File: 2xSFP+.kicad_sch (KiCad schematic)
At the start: 55 parts, among them J2 Bel-Fuse_SFP+_2x20_SS-79100-0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, U5 PCA9539AHF

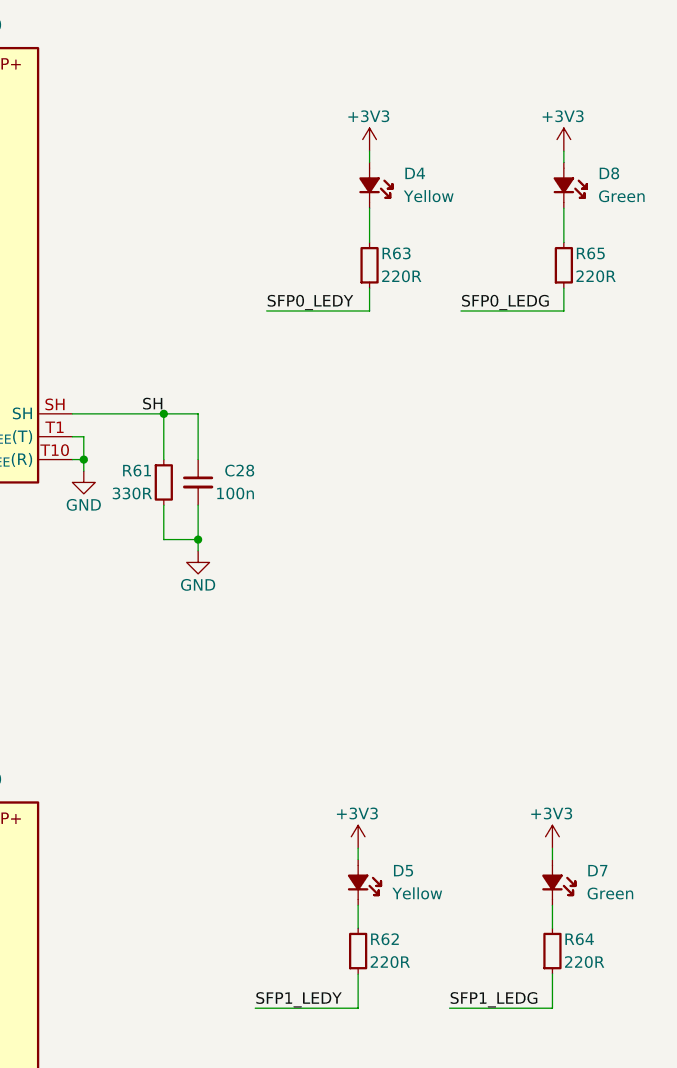
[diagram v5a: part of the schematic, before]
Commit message: [#66613] Change yellow LEDs from 0402 to 0603 package
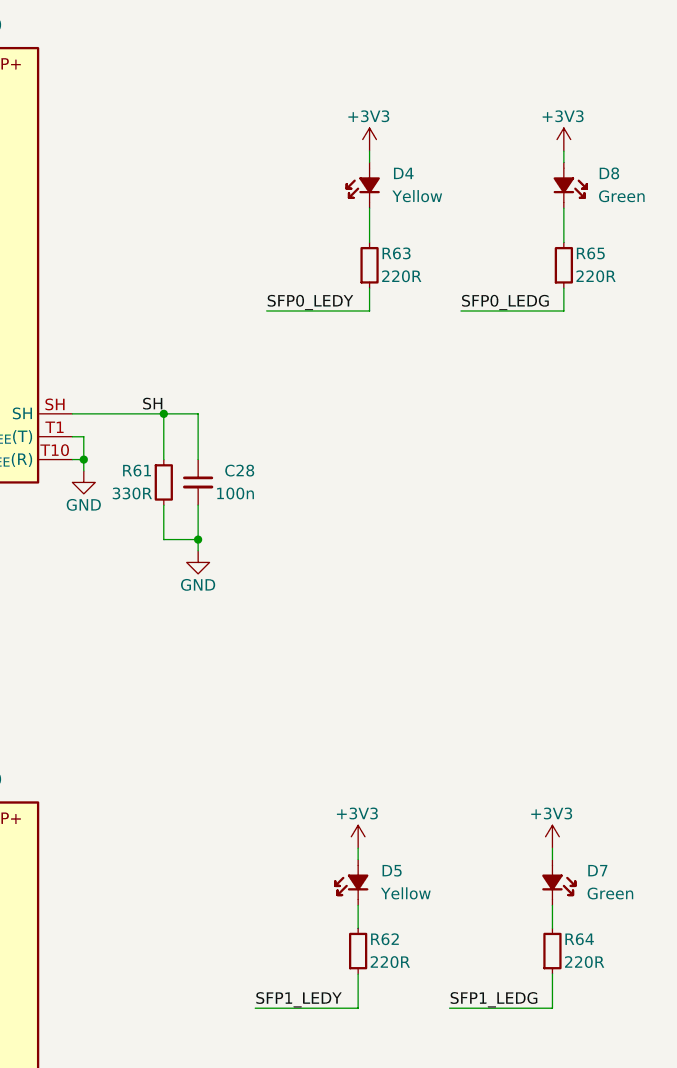
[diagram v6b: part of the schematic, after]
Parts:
- removed D4, D5: LED_Y_0402_VLMY1500-GS08, antmicro-footprints:LED_0402_1005Metric_Y, symbol antmicroLEDIndicationDiscrete:LED_Y_0402_VLMY1500-GS08
- added D4, D5: LED_Y_0603_LTST-C191KSKT, antmicro-footprints:LED_0603_1608Metric_Y, symbol antmicroLEDIndicationDiscrete:LED_Y_0603_LTST-C191KSKT
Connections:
- net +3V3: now also D4.2 (A), D5.2 (A)
- net at R63.2: now also D4.1 (C)
- net at R62.2: now also D5.1 (C)
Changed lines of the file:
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@@
+    )
+  )
+  (symbol (lib_id "antmicroLEDIndicationDiscrete:LED_Y_0603_LTST-C191KSKT") (at 322.58 76.2 90) (unit 1)
+    (in_bom yes) (on_board yes) (dnp no) (fields_autoplaced)
+    (property "Reference" "D4" (at 325.12 72.39 90)
+      (effects (font (size 1.27 1.27) (thickness 0.15)) (justify right))
+    )
+    (property "Value" "LED_Y_0603_LTST-C191KSKT" (at 330.2 53.34 0)
+      (effects (font (size 1.27 1.27) (thickness 0.15)) (justify left bottom) hide)
+    )
+    (property "Footprint" "antmicro-footprints:LED_0603_1608Metric_Y" (at 332.74 53.34 0)
+      (effects (font (size 1.27 1.27) (thickness 0.15)) (justify left bottom) hide)
+    )
+    (property "Datasheet" "https://optoelectronics.liteon.com/upload/download/DS22-2000-224/LTST-C191KSKT.PDF" (at 335.28 53.34 0)
+      (effects (font (size 1.27 1.27) (thickness 0.15)) (justify left bottom) hide)
+    )
+    (property "MPN" "LTST-C191KSKT" (at 337.82 53.34 0)
+      (effects (font (size 1.27 1.27) (thickness 0.15)) (justify left bottom) hide)
+    )
+    (property "Manufacturer" "Lite-On" (at 340.36 53.34 0)
+      (effects (font (size 1.27 1.27) (thickness 0.15)) (justify left bottom) hide)
+    )
+    (property "Color" "Yellow" (at 325.12 74.93 90)
+      (effects (font (size 1.27 1.27)) (justify right))
+    )
+    (property "Author" "Antmicro" (at 342.9 53.34 0)
+      (effects (font (size 1.27 1.27) (thickness 0.15)) (justify left bottom) hide)
+    )
+    (property "License" "Apache-2.0" (at 345.44 53.34 0)
+      (effects (font (size 1.27 1.27) (thickness 0.15)) (justify left bottom) hide)
+    )
+    (pin "1")
+    (pin "2")
+    (instances
+      (project "com-express-7-baseboard"
+        (path "/1b8c34da-dad5-4b0b-8c4b-45db766c4dfa/bc90cc14-34f1-4905-9b90-ab809e861ec6"
+          (reference "D4") (unit 1)
+        )
+      )
     )
   )
@@
     )
   )
+  (symbol (lib_id "antmicroLEDIndicationDiscrete:LED_Y_0603_LTST-C191KSKT") (at 321.31 153.67 90) (unit 1)
+    (in_bom yes) (on_board yes) (dnp no) (fields_autoplaced)
+    (property "Reference" "D5" (at 323.85 149.86 90)
+      (effects (font (size 1.27 1.27) (thickness 0.15)) (justify right))
+    )
+    (property "Value" "LED_Y_0603_LTST-C191KSKT" (at 328.93 130.81 0)
+      (effects (font (size 1.27 1.27) (thickness 0.15)) (justify left bottom) hide)
+    )
+    (property "Footprint" "antmicro-footprints:LED_0603_1608Metric_Y" (at 331.47 130.81 0)
+      (effects (font (size 1.27 1.27) (thickness 0.15)) (justify left bottom) hide)
+    )
+    (property "Datasheet" "https://optoelectronics.liteon.com/upload/download/DS22-2000-224/LTST-C191KSKT.PDF" (at 334.01 130.81 0)
+      (effects (font (size 1.27 1.27) (thickness 0.15)) (justify left bottom) hide)
+    )
+    (property "MPN" "LTST-C191KSKT" (at 336.55 130.81 0)
+      (effects (font (size 1.27 1.27) (thickness 0.15)) (justify left bottom) hide)
+    )
+    (property "Manufacturer" "Lite-On" (at 339.09 130.81 0)
+      (effects (font (size 1.27 1.27) (thickness 0.15)) (justify left bottom) hide)
+    )
+    (property "Color" "Yellow" (at 323.85 152.4 90)
+      (effects (font (size 1.27 1.27)) (justify right))
+    )
+    (property "Author" "Antmicro" (at 341.63 130.81 0)
+      (effects (font (size 1.27 1.27) (thickness 0.15)) (justify left bottom) hide)
+    )
+    (property "License" "Apache-2.0" (at 344.17 130.81 0)
+      (effects (font (size 1.27 1.27) (thickness 0.15)) (justify left bottom) hide)
+    )
+    (pin "1")
+    (pin "2")
+    (instances
+      (project "com-express-7-baseboard"
+        (path "/1b8c34da-dad5-4b0b-8c4b-45db766c4dfa/bc90cc14-34f1-4905-9b90-ab809e861ec6"
+          (reference "D5") (unit 1)
+        )
+      )
+    )
+  )
   (symbol (lib_id "antmicropower:+3V3") (at 232.41 118.11 0) (unit 1)
     (in_bom yes) (on_board yes) (dnp no) (fields_autoplaced)
@@
     )
   )
-  (symbol (lib_id "antmicroLEDIndicationDiscrete:LED_Y_0402_VLMY1500-GS08") (at 322.58 76.2 270) (mirror x) (unit 1)
-    (in_bom yes) (on_board yes) (dnp no) (fields_autoplaced)
-    (property "Reference" "D4" (at 326.39 72.39 90)
-      (effects (font (size 1.27 1.27) (thickness 0.15)) (justify left))
-    )
-    (property "Value" "LED_Y_0402_VLMY1500-GS08" (at 314.96 53.34 0)
-      (effects (font (size 1.27 1.27) (thickness 0.15)) (justify left bottom) hide)
-    )
-    (property "Footprint" "antmicro-footprints:LED_0402_1005Metric_Y" (at 312.42 53.34 0)
-      (effects (font (size 1.27 1.27) (thickness 0.15)) (justify left bottom) hide)
-    )
-    (property "Datasheet" "https://www.vishay.com/docs/82554/vlmo1500.pdf" (at 309.88 53.34 0)
-      (effects (font (size 1.27 1.27) (thickness 0.15)) (justify left bottom) hide)
-    )
-    (property "MPN" "VLMY1500-GS08" (at 307.34 53.34 0)
-      (effects (font (size 1.27 1.27) (thickness 0.15)) (justify left bottom) hide)
-    )
-    (property "Manufacturer" "Vishay" (at 304.8 53.34 0)
-      (effects (font (size 1.27 1.27) (thickness 0.15)) (justify left bottom) hide)
-    )
-    (property "Public" "False" (at 304.8 55.88 0)
-      (effects (font (size 1.27 1.27)) (justify left bottom) hide)
-    )
-    (property "Color" "Yellow" (at 326.39 74.93 90)
-      (effects (font (size 1.27 1.27)) (justify left))
-    )
-    (property "Author" "Antmicro" (at 302.26 53.34 0)
-      (effects (font (size 1.27 1.27) (thickness 0.15)) (justify left bottom) hide)
-    )
-    (property "License" "Apache-2.0" (at 299.72 53.34 0)
-      (effects (font (size 1.27 1.27) (thickness 0.15)) (justify left bottom) hide)
-    )
-    (pin "1")
-    (pin "2")
-    (instances
-      (project "com-express-7-baseboard"
-        (path "/1b8c34da-dad5-4b0b-8c4b-45db766c4dfa/bc90cc14-34f1-4905-9b90-ab809e861ec6"
-          (reference "D4") (unit 1)
-        )
-      )
-    )
-  )
   (symbol (lib_id "antmicropower:GND") (at 241.3 125.73 0) (mirror y) (unit 1)
     (in_bom yes) (on_board yes) (dnp no)
@@
         )
       )
-    )
-  )
-  (symbol (lib_id "antmicroLEDIndicationDiscrete:LED_Y_0402_VLMY1500-GS08") (at 321.31 153.67 270) (mirror x) (unit 1)
-    (in_bom yes) (on_board yes) (dnp no) (fields_autoplaced)
-    (property "Reference" "D5" (at 325.12 149.86 90)
-      (effects (font (size 1.27 1.27) (thickness 0.15)) (justify left))
-    )
-    (property "Value" "LED_Y_0402_VLMY1500-GS08" (at 313.69 130.81 0)
-      (effects (font (size 1.27 1.27) (thickness 0.15)) (justify left bottom) hide)
-    )
-    (property "Footprint" "antmicro-footprints:LED_0402_1005Metric_Y" (at 311.15 130.81 0)
-      (effects (font (size 1.27 1.27) (thickness 0.15)) (justify left bottom) hide)
-    )
-    (property "Datasheet" "https://www.vishay.com/docs/82554/vlmo1500.pdf" (at 308.61 130.81 0)
-      (effects (font (size 1.27 1.27) (thickness 0.15)) (justify left bottom) hide)
-    )
-    (property "MPN" "VLMY1500-GS08" (at 306.07 130.81 0)
-      (effects (font (size 1.27 1.27) (thickness 0.15)) (justify left bottom) hide)
-    )
-    (property "Manufacturer" "Vishay" (at 303.53 130.81 0)
-      (effects (font (size 1.27 1.27) (thickness 0.15)) (justify left bottom) hide)
-    )
-    (property "Public" "False" (at 303.53 133.35 0)
-      (effects (font (size 1.27 1.27)) (justify left bottom) hide)
-    )
-    (property "Color" "Yellow" (at 325.12 152.4 90)
-      (effects (font (size 1.27 1.27)) (justify left))
-    )
-    (property "Author" "Antmicro" (at 300.99 130.81 0)
-      (effects (font (size 1.27 1.27) (thickness 0.15)) (justify left bottom) hide)
-    )
-    (property "License" "Apache-2.0" (at 298.45 130.81 0)
-      (effects (font (size 1.27 1.27) (thickness 0.15)) (justify left bottom) hide)
-    )
-    (pin "1")
-    (pin "2")
-    (instances
-      (project "com-express-7-baseboard"
-        (path "/1b8c34da-dad5-4b0b-8c4b-45db766c4dfa/bc90cc14-34f1-4905-9b90-ab809e861ec6"
-          (reference "D5") (unit 1)
-        )
-      )

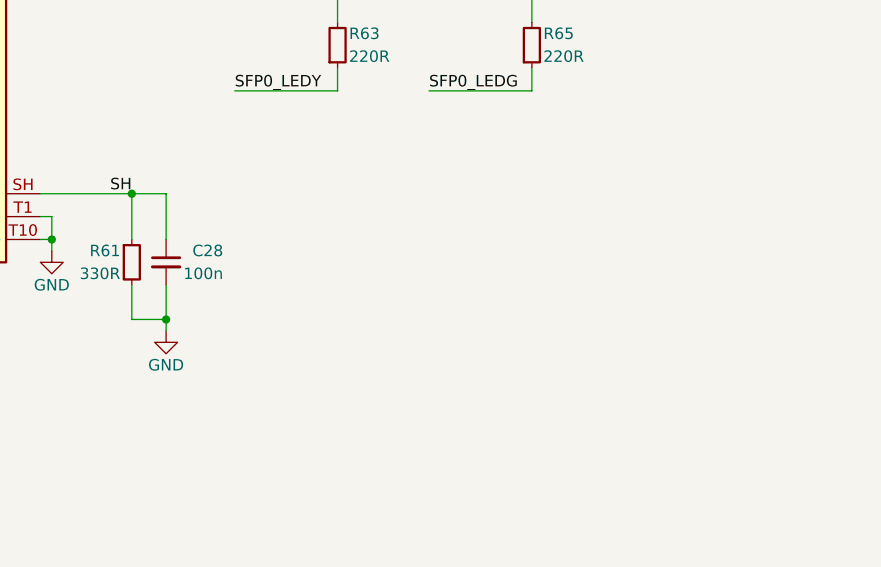
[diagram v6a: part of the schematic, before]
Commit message: [#66613] Add more capacitors to SFP connector shield
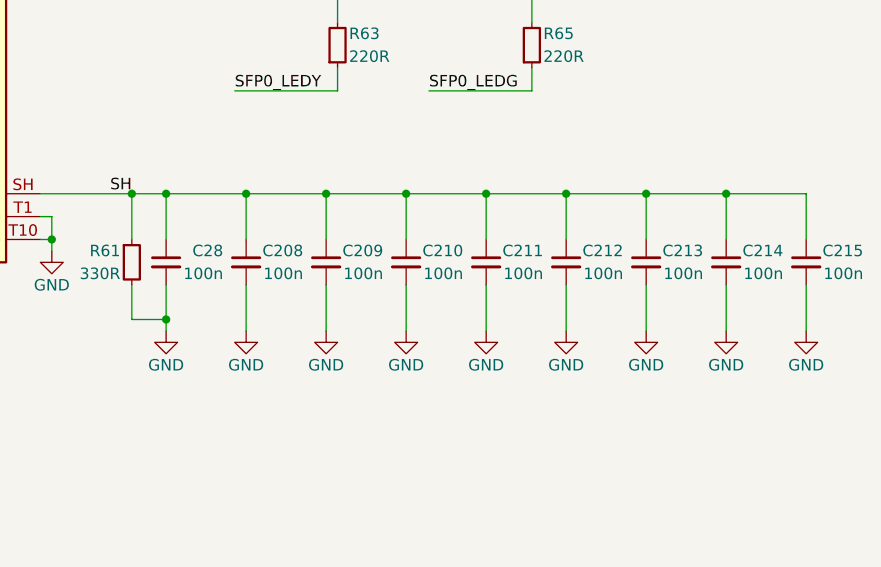
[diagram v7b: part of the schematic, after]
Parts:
- added C208, C209, C210, C211, C212, C213, C214, C215: C_100n_0402, antmicro-footprints:C_0402_1005Metric, symbol antmicroCapacitors0402:C_100n_0402
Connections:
- net GND: now also C208.2, C209.2, C210.2, C211.2, C212.2, C213.2, C214.2, C215.2
- net SH: now also C208.1, C209.1, C210.1, C211.1, C212.1, C213.1, C214.1, C215.1

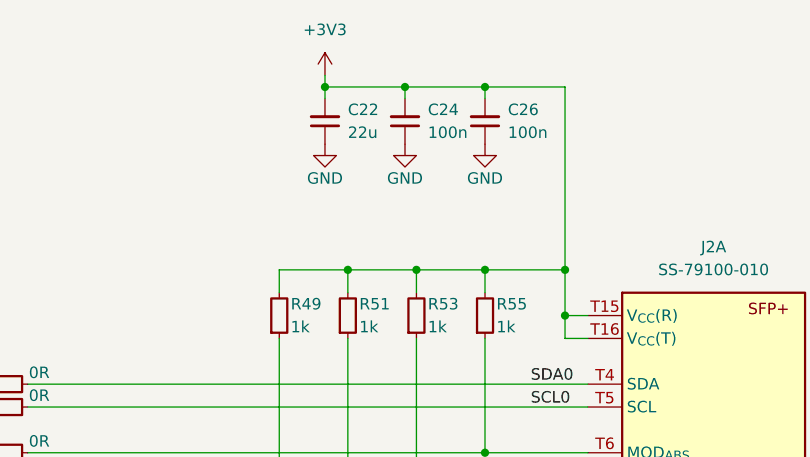
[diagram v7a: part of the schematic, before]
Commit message: [#66613] Fix ERC, adjust overlapping text on schematic
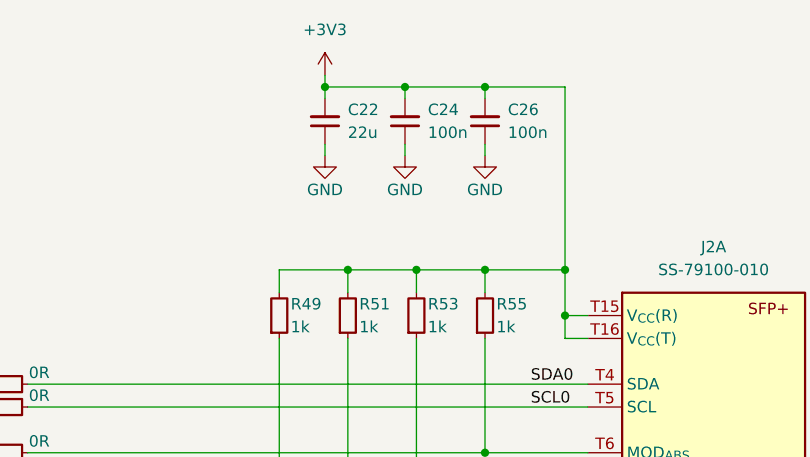
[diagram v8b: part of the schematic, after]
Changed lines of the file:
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@@
+    (stroke (width 0) (type default))
+  )
+  (wire (pts (xy 241.3 43.18) (xy 241.3 41.91))
     (stroke (width 0) (type default))
   )
@@
     (stroke (width 0) (type default))
   )
+  (wire (pts (xy 250.19 43.18) (xy 250.19 41.91))
+    (stroke (width 0) (type default))
+  )
   (wire (pts (xy 241.3 119.38) (xy 241.3 120.65))
     (stroke (width 0) (type default))
@@
   )
   (bus (pts (xy 176.53 151.13) (xy 176.53 153.67))
+    (stroke (width 0) (type default))
+  )
+  (wire (pts (xy 232.41 43.18) (xy 232.41 41.91))
     (stroke (width 0) (type default))
   )
@@
     )
   )
-  (symbol (lib_id "antmicropower:GND") (at 241.3 41.91 0) (mirror y) (unit 1)
-    (in_bom yes) (on_board yes) (dnp no)
-    (property "Reference" "#PWR044" (at 232.41 44.45 0)
-      (effects (font (size 1.27 1.27) (thickness 0.15)) (justify left bottom) hide)
-    )
-    (property "Value" "GND" (at 241.3 45.72 0)
-      (effects (font (size 1.27 1.27) (thickness 0.15)))
-    )
-    (property "Footprint" "" (at 232.41 49.53 0)
-      (effects (font (size 1.27 1.27) (thickness 0.15)) (justify left bottom) hide)
-    )
-    (property "Datasheet" "" (at 232.41 54.61 0)
-      (effects (font (size 1.27 1.27) (thickness 0.15)) (justify left bottom) hide)
-    )
-    (property "Author" "Antmicro" (at 232.41 49.53 0)
-      (effects (font (size 1.27 1.27) (thickness 0.15)) (justify left bottom) hide)
-    )
-    (property "License" "Apache-2.0" (at 232.41 52.07 0)
+  (symbol (lib_id "antmicropower:GND") (at 241.3 43.18 0) (mirror y) (unit 1)
+    (in_bom yes) (on_board yes) (dnp no)
+    (property "Reference" "#PWR044" (at 232.41 45.72 0)
+      (effects (font (size 1.27 1.27) (thickness 0.15)) (justify left bottom) hide)
+    )
+    (property "Value" "GND" (at 241.3 46.99 0)
+      (effects (font (size 1.27 1.27) (thickness 0.15)))
+    )
+    (property "Footprint" "" (at 232.41 50.8 0)
+      (effects (font (size 1.27 1.27) (thickness 0.15)) (justify left bottom) hide)
+    )
+    (property "Datasheet" "" (at 232.41 55.88 0)
+      (effects (font (size 1.27 1.27) (thickness 0.15)) (justify left bottom) hide)
+    )
+    (property "Author" "Antmicro" (at 232.41 50.8 0)
+      (effects (font (size 1.27 1.27) (thickness 0.15)) (justify left bottom) hide)
+    )
+    (property "License" "Apache-2.0" (at 232.41 53.34 0)
       (effects (font (size 1.27 1.27) (thickness 0.15)) (justify left bottom) hide)
     )
@@
     )
   )
-  (symbol (lib_id "antmicropower:GND") (at 250.19 41.91 0) (mirror y) (unit 1)
-    (in_bom yes) (on_board yes) (dnp no)
-    (property "Reference" "#PWR048" (at 241.3 44.45 0)
-      (effects (font (size 1.27 1.27) (thickness 0.15)) (justify left bottom) hide)
-    )
-    (property "Value" "GND" (at 250.19 45.72 0)
-      (effects (font (size 1.27 1.27) (thickness 0.15)))
-    )
-    (property "Footprint" "" (at 241.3 49.53 0)
-      (effects (font (size 1.27 1.27) (thickness 0.15)) (justify left bottom) hide)
-    )
-    (property "Datasheet" "" (at 241.3 54.61 0)
-      (effects (font (size 1.27 1.27) (thickness 0.15)) (justify left bottom) hide)
-    )
-    (property "Author" "Antmicro" (at 241.3 49.53 0)
-      (effects (font (size 1.27 1.27) (thickness 0.15)) (justify left bottom) hide)
-    )
-    (property "License" "Apache-2.0" (at 241.3 52.07 0)
+  (symbol (lib_id "antmicropower:GND") (at 250.19 43.18 0) (mirror y) (unit 1)
+    (in_bom yes) (on_board yes) (dnp no)
+    (property "Reference" "#PWR048" (at 241.3 45.72 0)
+      (effects (font (size 1.27 1.27) (thickness 0.15)) (justify left bottom) hide)
+    )
+    (property "Value" "GND" (at 250.19 46.99 0)
+      (effects (font (size 1.27 1.27) (thickness 0.15)))
+    )
+    (property "Footprint" "" (at 241.3 50.8 0)
+      (effects (font (size 1.27 1.27) (thickness 0.15)) (justify left bottom) hide)
+    )
+    (property "Datasheet" "" (at 241.3 55.88 0)
+      (effects (font (size 1.27 1.27) (thickness 0.15)) (justify left bottom) hide)
+    )
+    (property "Author" "Antmicro" (at 241.3 50.8 0)
+      (effects (font (size 1.27 1.27) (thickness 0.15)) (justify left bottom) hide)
+    )
+    (property "License" "Apache-2.0" (at 241.3 53.34 0)
       (effects (font (size 1.27 1.27) (thickness 0.15)) (justify left bottom) hide)
     )
@@
     )
   )
-  (symbol (lib_id "antmicropower:GND") (at 232.41 41.91 0) (mirror y) (unit 1)
-    (in_bom yes) (on_board yes) (dnp no)
-    (property "Reference" "#PWR041" (at 223.52 44.45 0)
-      (effects (font (size 1.27 1.27) (thickness 0.15)) (justify left bottom) hide)
-    )
-    (property "Value" "GND" (at 232.41 45.72 0)
-      (effects (font (size 1.27 1.27) (thickness 0.15)))
-    )
-    (property "Footprint" "" (at 223.52 49.53 0)
-      (effects (font (size 1.27 1.27) (thickness 0.15)) (justify left bottom) hide)
-    )
-    (property "Datasheet" "" (at 223.52 54.61 0)
-      (effects (font (size 1.27 1.27) (thickness 0.15)) (justify left bottom) hide)
-    )
-    (property "Author" "Antmicro" (at 223.52 49.53 0)
-      (effects (font (size 1.27 1.27) (thickness 0.15)) (justify left bottom) hide)
-    )
-    (property "License" "Apache-2.0" (at 223.52 52.07 0)
-      (effects (font (size 1.27 1.27) (thickness 0.15)) (justify left bottom) hide)
-    )
+  (symbol (lib_id "antmicropower:GND") (at 232.41 43.18 0) (mirror y) (unit 1)
+    (in_bom yes) (on_board yes) (dnp no)
+    (property "Reference" "#PWR041" (at 223.52 45.72 0)
+      (effects (font (size 1.27 1.27) (thickness 0.15)) (justify left bottom) hide)
+    )
+    (property "Value" "GND" (at 232.41 46.99 0)
+      (effects (font (size 1.27 1.27) (thickness 0.15)))
+    )
+    (property "Footprint" "" (at 223.52 50.8 0)
+      (effects (font (size 1.27 1.27) (thickness 0.15)) (justify left bottom) hide)
+    )
+    (property "Datasheet" "" (at 223.52 55.88 0)
+      (effects (font (size 1.27 1.27) (thickness 0.15)) (justify left bottom) hide)
+    )
+    (property "Author" "Antmicro" (at 223.52 50.8 0)
+      (effects (font (size 1.27 1.27) (thickness 0.15)) (justify left bottom) hide)
+    )
+    (property "License" "Apache-2.0" (at 223.52 53.34 0)
+      (effects (font (size 1.27 1.27) (thickness 0.15)) (justify left bottom) hide)
+    )
